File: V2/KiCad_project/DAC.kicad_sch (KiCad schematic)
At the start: 62 parts, among them Q301 MMBT3906, U301 OPA2673IRGVR, U303 NE5532DR

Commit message: Fix rotation for JLCPCB
Add `FT Rotation Offset` fields to components that have a wrong
rotation when ordering from JLCPCB.
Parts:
- D301, D302, Q301: FT Rotation Offset (none) -> 180
- U303: FT Rotation Offset (none) -> 90
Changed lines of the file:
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@@
 			)
 		)
+		(property "FT Rotation Offset" "180"
+			(at 110.49 130.81 0)
+			(effects
+				(font
+					(size 1.27 1.27)
+				)
+				(hide yes)
+			)
+		)
 		(pin "1"
 		)
@@
 			)
 		)
+		(property "FT Rotation Offset" "180"
+			(at 50.8 130.81 90)
+			(effects
+				(font
+					(size 1.27 1.27)
+				)
+				(hide yes)
+			)
+		)
 		(pin "1"
 		)
@@
 			)
 		)
+		(property "FT Rotation Offset" "90"
+			(at 139.7 130.81 0)
+			(effects
+				(font
+					(size 1.27 1.27)
+				)
+				(hide yes)
+			)
+		)
 		(pin "7"
 		)
@@
 			)
 		)
+		(property "FT Rotation Offset" "180"
+			(at 106.68 110.49 0)
+			(effects
+				(font
+					(size 1.27 1.27)
+				)
+				(hide yes)
+			)
+		)

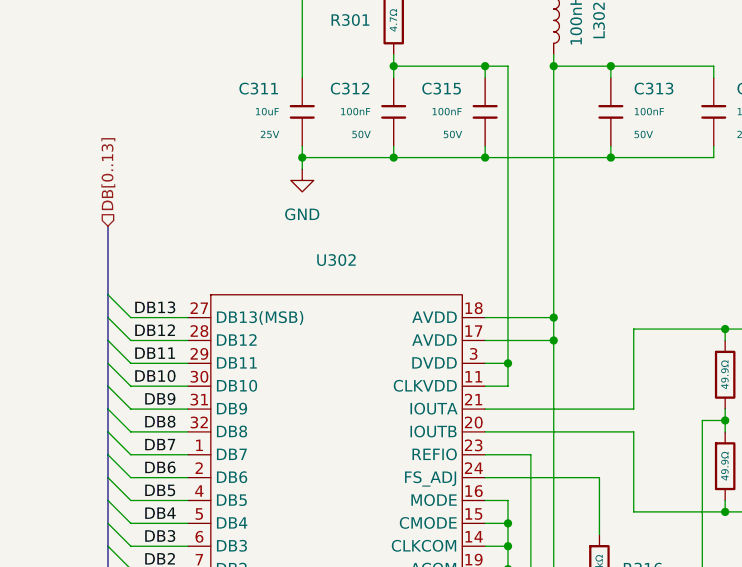
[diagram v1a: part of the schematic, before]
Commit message: Added ordering number to value of U201, U202 and U302 because it did not appear in schematic.pdf and in bom.csv
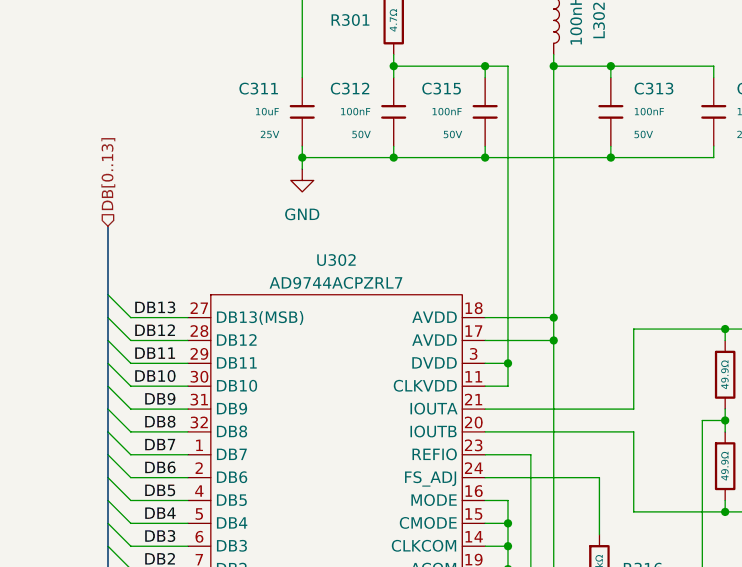
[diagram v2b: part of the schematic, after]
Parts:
- U302: value ~ -> AD9744ACPZRL7
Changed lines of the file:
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@@
 			)
 		)
-		(property "Value" "~"
+		(property "Value" "AD9744ACPZRL7"
 			(at 46.99 67.31 0)
 			(effects
